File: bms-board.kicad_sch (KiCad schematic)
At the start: 1 part, among them U1 LTC6804-2

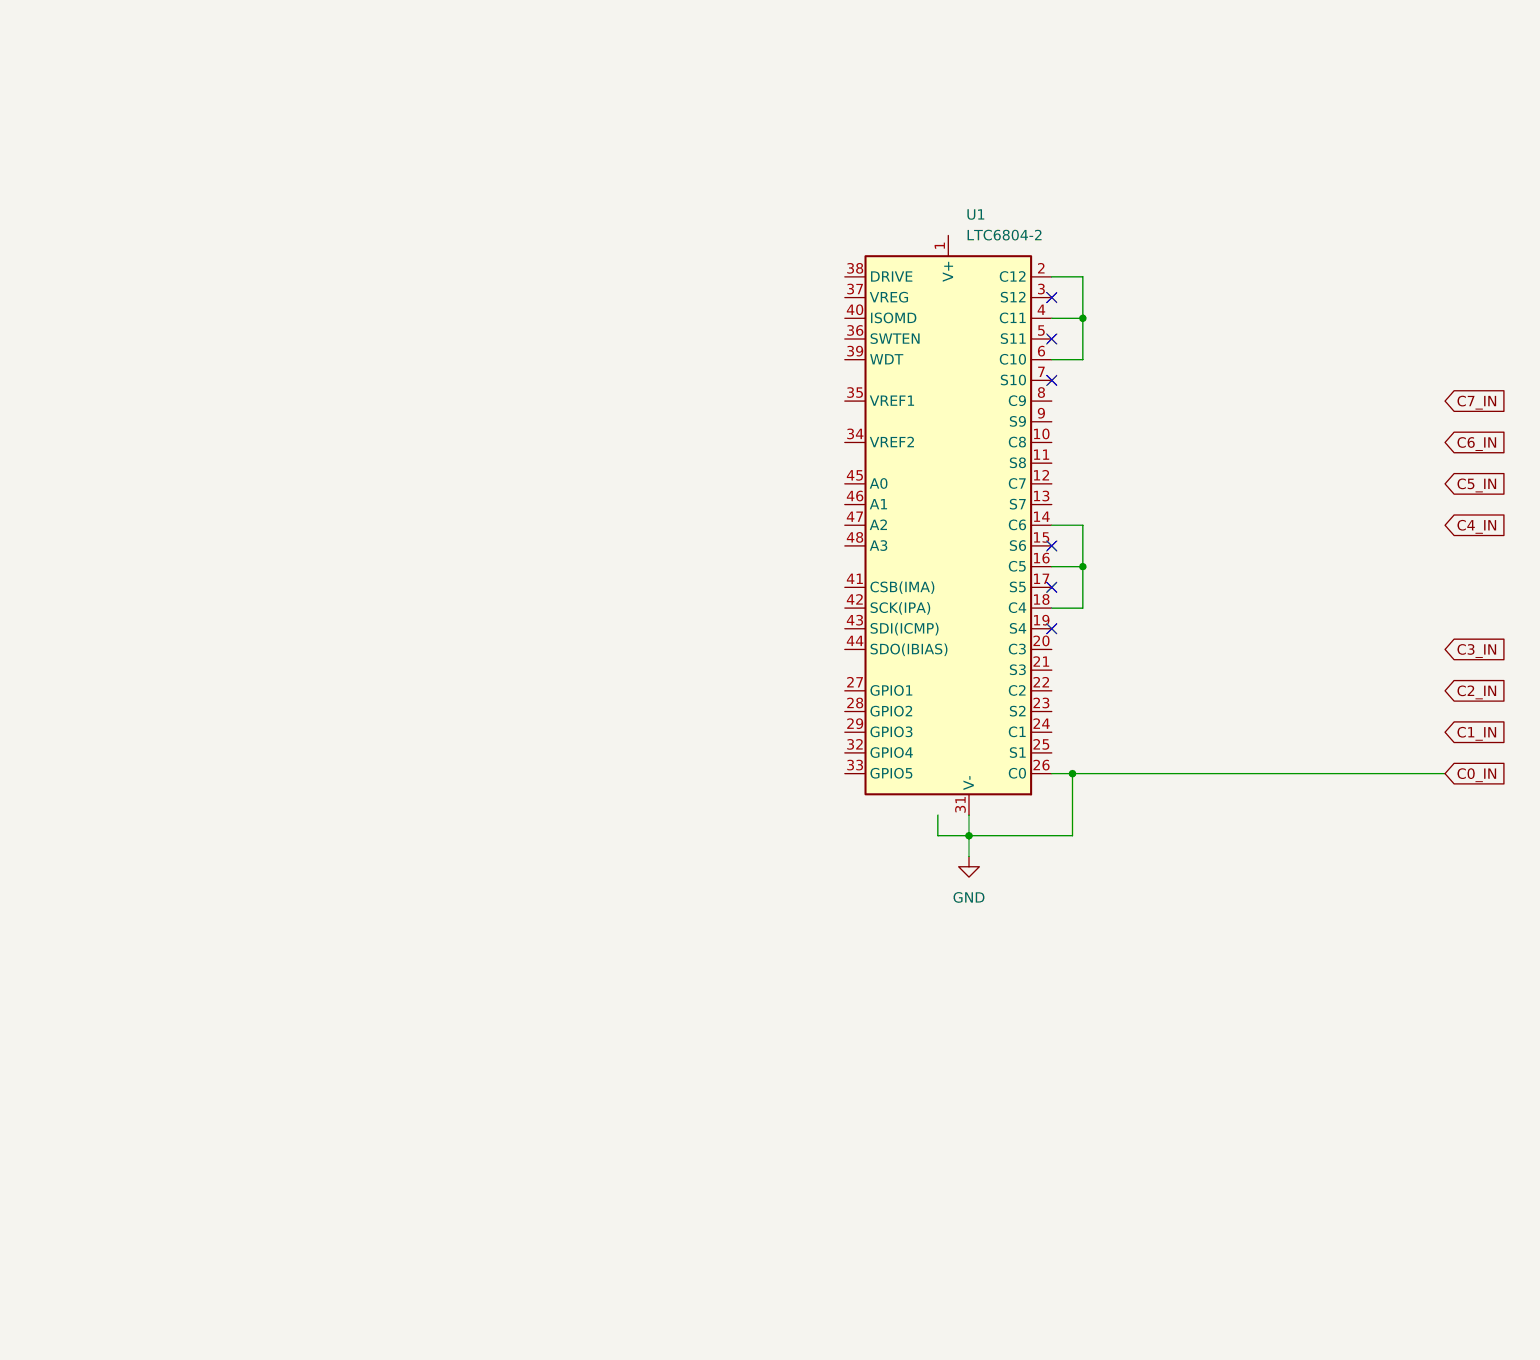
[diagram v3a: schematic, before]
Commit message: feat: add schematic hierarchy
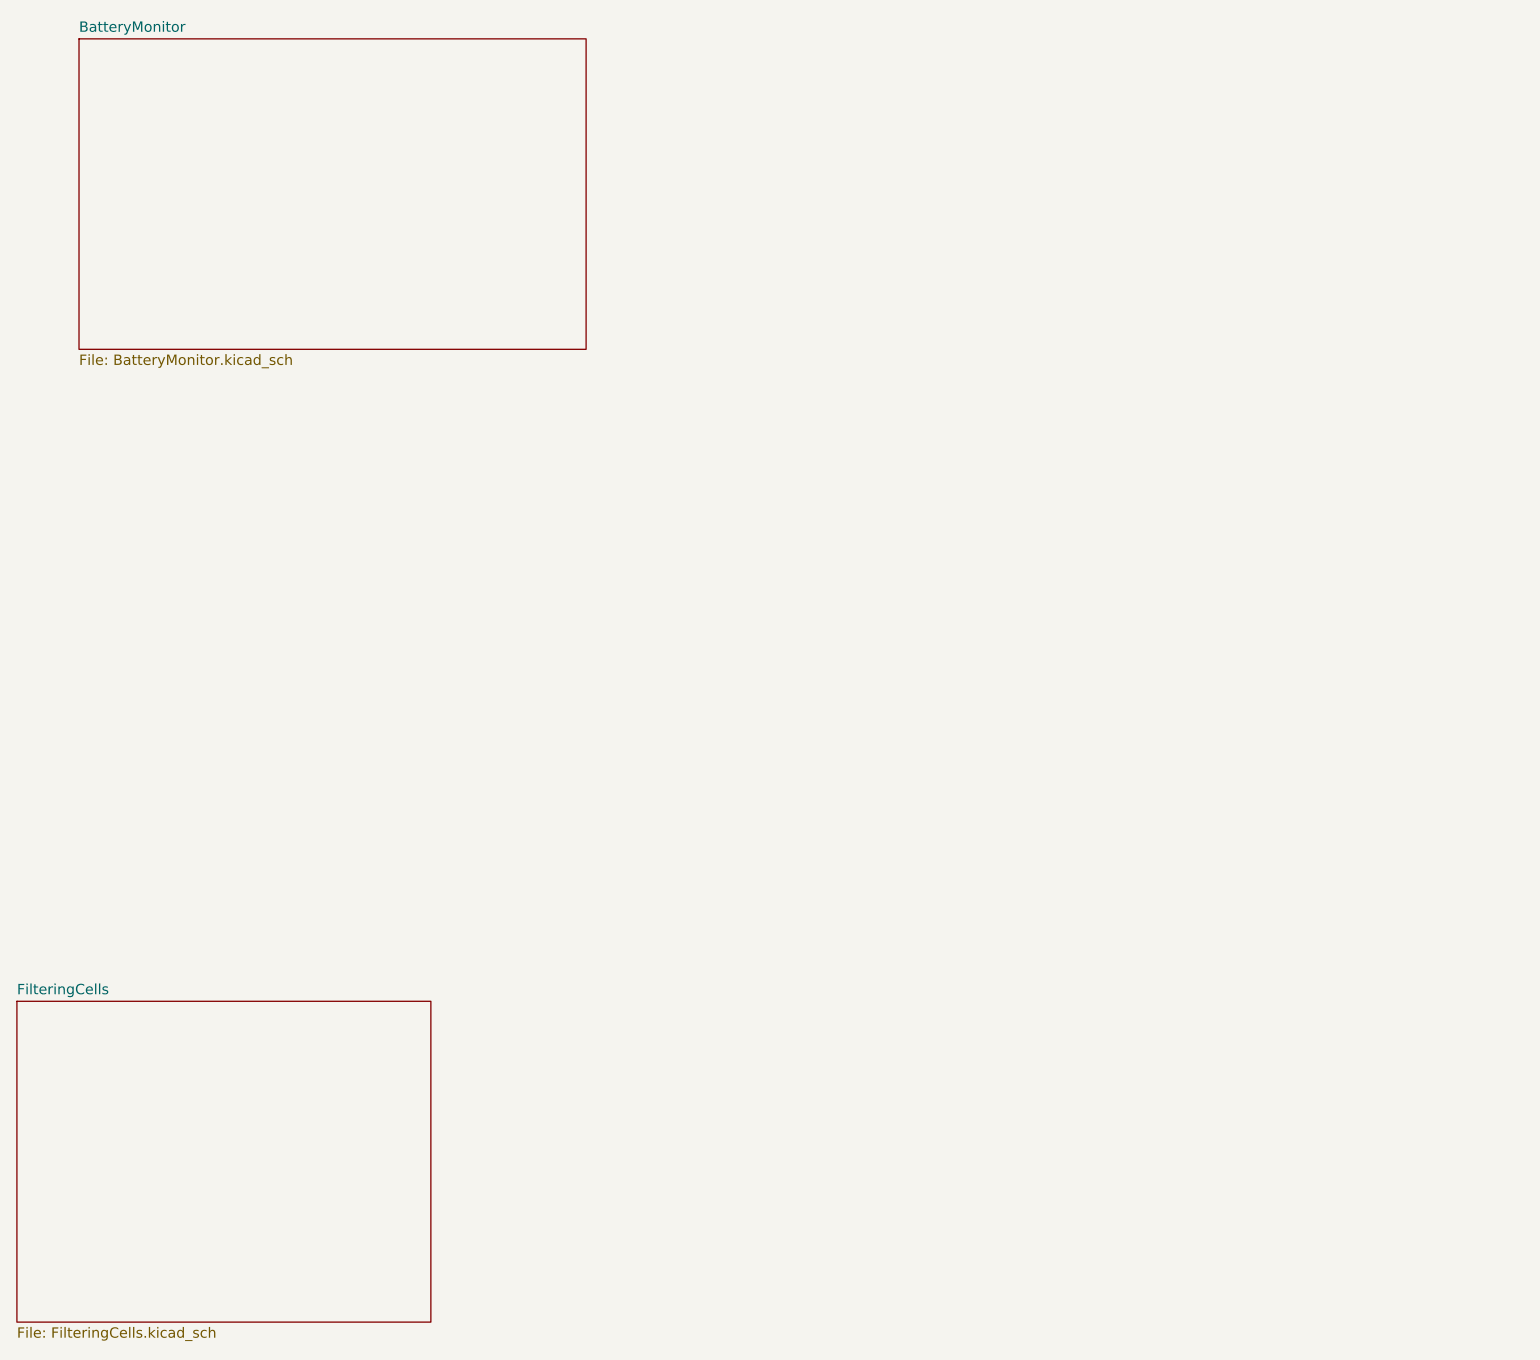
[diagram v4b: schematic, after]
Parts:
- removed U1: LTC6804-2, Package_SO:SSOP-48_5.3x12.8mm_P0.5mm, symbol FixedWing:LTC6804-2
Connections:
- no-connect marks 6 -> 0
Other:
- added sheet BatteryMonitor (BatteryMonitor.kicad_sch)
- added sheet FilteringCells (FilteringCells.kicad_sch)
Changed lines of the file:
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@@
 (kicad_sch (version 20230121) (generator eeschema)
   (paper "A4")
-  (junction (at 158.75 62.23) (diameter 0) (color 0 0 0 0)
-  )
-  (junction (at 157.48 118.11) (diameter 0) (color 0 0 0 0)
-  )
-  (junction (at 158.75 92.71) (diameter 0) (color 0 0 0 0)
-  )
-  (junction (at 144.78 125.73) (diameter 0) (color 0 0 0 0)
-  )
-  (no_connect (at 154.94 64.77))
-  (no_connect (at 154.94 90.17))
-  (no_connect (at 154.94 95.25))
-  (no_connect (at 154.94 69.85))
-  (no_connect (at 154.94 100.33))
-  (no_connect (at 154.94 59.69))
-  (wire (pts (xy 154.94 57.15) (xy 158.75 57.15))
-    (stroke (width 0) (type default))
-  )
-  (wire (pts (xy 144.78 128.27) (xy 144.78 125.73))
-    (stroke (width 0) (type default))
-  )
-  (wire (pts (xy 157.48 118.11) (xy 203.2 118.11))
-    (stroke (width 0) (type default))
-  )
-  (wire (pts (xy 158.75 57.15) (xy 158.75 62.23))
-    (stroke (width 0) (type default))
-  )
-  (wire (pts (xy 158.75 92.71) (xy 158.75 97.79))
-    (stroke (width 0) (type default))
-  )
-  (wire (pts (xy 144.78 125.73) (xy 157.48 125.73))
-    (stroke (width 0) (type default))
-  )
-  (wire (pts (xy 154.94 67.31) (xy 158.75 67.31))
-    (stroke (width 0) (type default))
-  )
-  (wire (pts (xy 154.94 62.23) (xy 158.75 62.23))
-    (stroke (width 0) (type default))
-  )
-  (wire (pts (xy 158.75 87.63) (xy 158.75 92.71))
-    (stroke (width 0) (type default))
-  )
-  (wire (pts (xy 154.94 97.79) (xy 158.75 97.79))
-    (stroke (width 0) (type default))
-  )
-  (wire (pts (xy 144.78 125.73) (xy 144.78 123.19))
-    (stroke (width 0) (type default))
-  )
-  (wire (pts (xy 154.94 92.71) (xy 158.75 92.71))
-    (stroke (width 0) (type default))
-  )
-  (wire (pts (xy 154.94 87.63) (xy 158.75 87.63))
-    (stroke (width 0) (type default))
-  )
-  (wire (pts (xy 154.94 118.11) (xy 157.48 118.11))
-    (stroke (width 0) (type default))
-  )
-  (wire (pts (xy 140.97 125.73) (xy 140.97 123.19))
-    (stroke (width 0) (type default))
-  )
-  (wire (pts (xy 158.75 62.23) (xy 158.75 67.31))
-    (stroke (width 0) (type default))
-  )
-  (wire (pts (xy 157.48 118.11) (xy 157.48 125.73))
-    (stroke (width 0) (type default))
-  )
-  (wire (pts (xy 140.97 125.73) (xy 144.78 125.73))
-    (stroke (width 0) (type default))
-  )
-  (global_label "C1_IN" (shape input) (at 203.2 113.03 0) (fields_autoplaced)
-    (effects (font (size 1.27 1.27)) (justify left))
-    (property "Intersheetrefs" "${INTERSHEET_REFS}" (at 211.5676 113.03 0)
-      (effects (font (size 1.27 1.27)) (justify left) hide)
+  (sheet (at 35.56 27.94) (size 62.23 38.1) (fields_autoplaced)
+    (stroke (width 0.1524) (type solid))
+    (fill (color 0 0 0 0.0000))
+    (property "Sheetname" "BatteryMonitor" (at 35.56 27.2284 0)
+      (effects (font (size 1.27 1.27)) (justify left bottom))
     )
-  )
-  (global_label "C0_IN" (shape input) (at 203.2 118.11 0) (fields_autoplaced)
-    (effects (font (size 1.27 1.27)) (justify left))
-    (property "Intersheetrefs" "${INTERSHEET_REFS}" (at 211.5676 118.11 0)
-      (effects (font (size 1.27 1.27)) (justify left) hide)
+    (property "Sheetfile" "BatteryMonitor.kicad_sch" (at 35.56 66.6246 0)
+      (effects (font (size 1.27 1.27)) (justify left top))
     )
-  )
-  (global_label "C2_IN" (shape input) (at 203.2 107.95 0) (fields_autoplaced)
-    (effects (font (size 1.27 1.27)) (justify left))
-    (property "Intersheetrefs" "${INTERSHEET_REFS}" (at 211.5676 107.95 0)
-      (effects (font (size 1.27 1.27)) (justify left) hide)
-    )
-  )
-  (global_label "C5_IN" (shape input) (at 203.2 82.55 0) (fields_autoplaced)
-    (effects (font (size 1.27 1.27)) (justify left))
-    (property "Intersheetrefs" "${INTERSHEET_REFS}" (at 211.5676 82.55 0)
-      (effects (font (size 1.27 1.27)) (justify left) hide)
-    )
-  )
-  (global_label "C6_IN" (shape input) (at 203.2 77.47 0) (fields_autoplaced)
-    (effects (font (size 1.27 1.27)) (justify left))
-    (property "Intersheetrefs" "${INTERSHEET_REFS}" (at 211.5676 77.47 0)
-      (effects (font (size 1.27 1.27)) (justify left) hide)
-    )
-  )
-  (global_label "C4_IN" (shape input) (at 203.2 87.63 0) (fields_autoplaced)
-    (effects (font (size 1.27 1.27)) (justify left))
-    (property "Intersheetrefs" "${INTERSHEET_REFS}" (at 211.5676 87.63 0)
-      (effects (font (size 1.27 1.27)) (justify left) hide)
-    )
-  )
-  (global_label "C7_IN" (shape input) (at 203.2 72.39 0) (fields_autoplaced)
-    (effects (font (size 1.27 1.27)) (justify left))
-    (property "Intersheetrefs" "${INTERSHEET_REFS}" (at 211.5676 72.39 0)
-      (effects (font (size 1.27 1.27)) (justify left) hide)
-    )
-  )
-  (global_label "C3_IN" (shape input) (at 203.2 102.87 0) (fields_autoplaced)
-    (effects (font (size 1.27 1.27)) (justify left))
-    (property "Intersheetrefs" "${INTERSHEET_REFS}" (at 211.5676 102.87 0)
-      (effects (font (size 1.27 1.27)) (justify left) hide)
-    )
-  )
-  (symbol (lib_name "LTC6804-2_1") (lib_id "FixedWing:LTC6804-2") (at 142.24 87.63 0) (unit 1)
-    (in_bom yes) (on_board yes) (dnp no) (fields_autoplaced)
-    (property "Reference" "U1" (at 144.4341 49.53 0)
-      (effects (font (size 1.27 1.27)) (justify left))
-    )
-    (property "Value" "LTC6804-2" (at 144.4341 52.07 0)
-      (effects (font (size 1.27 1.27)) (justify left))
-    )
-    (property "Footprint" "Package_SO:SSOP-48_5.3x12.8mm_P0.5mm" (at 142.24 124.46 0)
-      (effects (font (size 1.27 1.27)) hide)
-    )
-    (property "Datasheet" "https://www.analog.com/media/en/technical-documentation/data-sheets/680412fc.pdf" (at 156.21 53.34 0)
-      (effects (font (size 1.27 1.27)) hide)
-    )
-    (pin "31")
-    (pin "36")
-    (pin "37")
-    (pin "18")
-    (pin "48")
-    (pin "5")
-    (pin "6")
-    (pin "23")
-    (pin "1")
-    (pin "34")
-    (pin "10")
-    (pin "26")
-    (pin "22")
-    (pin "29")
-    (pin "32")
-    (pin "14")
-    (pin "16")
-    (pin "2")
-    (pin "44")
-    (pin "11")
-    (pin "42")
-    (pin "7")
-    (pin "8")
-    (pin "9")
-    (pin "17")
-    (pin "24")
-    (pin "39")
-    (pin "21")
-    (pin "43")
-    (pin "19")
-    (pin "40")
-    (pin "35")
-    (pin "30")
-    (pin "45")
-    (pin "15")
-    (pin "25")
-    (pin "28")
-    (pin "46")
-    (pin "38")
-    (pin "20")
-    (pin "12")
-    (pin "3")
-    (pin "41")
-    (pin "4")
-    (pin "33")
-    (pin "13")
-    (pin "27")
-    (pin "47")
     (instances
       (project "bms-board"
-        (path "/8a7831d1-a913-4f04-8780-225d2234b41d"
-          (reference "U1") (unit 1)
-        )
+        (path "/8a7831d1-a913-4f04-8780-225d2234b41d" (page "3"))
       )
     )
   )
-  (symbol (lib_id "power:GND") (at 144.78 128.27 0) (unit 1)
-    (in_bom yes) (on_board yes) (dnp no) (fields_autoplaced)
-    (property "Reference" "#PWR01" (at 144.78 134.62 0)
-      (effects (font (size 1.27 1.27)) hide)
+  (sheet (at 27.94 146.05) (size 50.8 39.37) (fields_autoplaced)
+    (stroke (width 0.1524) (type solid))
+    (fill (color 0 0 0 0.0000))
+    (property "Sheetname" "FilteringCells" (at 27.94 145.3384 0)
+      (effects (font (size 1.27 1.27)) (justify left bottom))
     )
-    (property "Value" "GND" (at 144.78 133.35 0)
-      (effects (font (size 1.27 1.27)))
+    (property "Sheetfile" "FilteringCells.kicad_sch" (at 27.94 186.0046 0)
+      (effects (font (size 1.27 1.27)) (justify left top))
     )
-    (property "Footprint" "" (at 144.78 128.27 0)
-      (effects (font (size 1.27 1.27)) hide)
-    )
-    (property "Datasheet" "" (at 144.78 128.27 0)
-      (effects (font (size 1.27 1.27)) hide)
-    )
-    (pin "1")
     (instances
       (project "bms-board"
-        (path "/8a7831d1-a913-4f04-8780-225d2234b41d"
-          (reference "#PWR01") (unit 1)
-        )
+        (path "/8a7831d1-a913-4f04-8780-225d2234b41d" (page "2"))
       )
     )

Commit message: feat: resolved splitting cells across monitor
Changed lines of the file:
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@@
 (kicad_sch (version 20230121) (generator eeschema)
-  (paper "A4")
-  (sheet (at 35.56 27.94) (size 62.23 38.1) (fields_autoplaced)
+  (paper "B")
+  (sheet (at 116.84 69.85) (size 62.23 38.1) (fields_autoplaced)
     (stroke (width 0.1524) (type solid))
     (fill (color 0 0 0 0.0000))
-    (property "Sheetname" "BatteryMonitor" (at 35.56 27.2284 0)
+    (property "Sheetname" "BatteryMonitor" (at 116.84 69.1384 0)
       (effects (font (size 1.27 1.27)) (justify left bottom))
     )
-    (property "Sheetfile" "BatteryMonitor.kicad_sch" (at 35.56 66.6246 0)
+    (property "Sheetfile" "BatteryMonitor.kicad_sch" (at 116.84 108.5346 0)
       (effects (font (size 1.27 1.27)) (justify left top))
     )
@@
     )
   )
-  (sheet (at 27.94 146.05) (size 50.8 39.37) (fields_autoplaced)
+  (sheet (at 34.29 69.85) (size 50.8 39.37) (fields_autoplaced)
     (stroke (width 0.1524) (type solid))
     (fill (color 0 0 0 0.0000))
-    (property "Sheetname" "FilteringCells" (at 27.94 145.3384 0)
+    (property "Sheetname" "FilteringCells" (at 34.29 69.1384 0)
       (effects (font (size 1.27 1.27)) (justify left bottom))
     )
-    (property "Sheetfile" "FilteringCells.kicad_sch" (at 27.94 186.0046 0)
+    (property "Sheetfile" "FilteringCells.kicad_sch" (at 34.29 109.8046 0)
       (effects (font (size 1.27 1.27)) (justify left top))
     )
